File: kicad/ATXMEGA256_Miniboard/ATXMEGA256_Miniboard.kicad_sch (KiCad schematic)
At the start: 26 parts, among them J1 2x5 IDC Socket, J10 1x2 Goldpin Header, J11 2x5 Goldpin Socket, J12 1x2 Goldpin Header, J13 USB micro B 2.0 Socket, J14 2x3 Goldpin Socket, J15 2x3 Goldpin Socket, J2 1x2 Screw Terminal, J3 2x3 Goldpin Header, J4 2x5 Goldpin Socket, J5 2x5 Goldpin Socket, J6 2x5 Goldpin Socket, J7 2x3 Goldpin Socket, J8 2x5 Goldpin Socket, J9 1x2 Goldpin Header, SW1 RESET, U1 ATXMEGA256A3B-AU, Y1 32.768 kHz, Y2 16 MHz

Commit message: rev 1.1
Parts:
- removed J10, J12, J9: 1x2 Goldpin Header, Connector_PinHeader_2.54mm:PinHeader_1x02_P2.54mm_Vertical, symbol Connector:Conn_01x02_Pin
- removed J11, J4, J5, J6, J8: 2x5 Goldpin Socket, Connector_PinSocket_2.54mm:PinSocket_2x05_P2.54mm_Vertical_SMD, symbol Connector_Generic:Conn_02x05_Odd_Even
- removed J13: USB micro B 2.0 Socket, Connector_USB:USB_Micro-B_Amphenol_10118193-0001LF_Horizontal, symbol Connector:USB_B_Micro
- removed J14, J7: 2x3 Goldpin Socket, Connector_PinSocket_2.54mm:PinSocket_2x03_P2.54mm_Vertical_SMD, symbol Connector_Generic:Conn_02x03_Odd_Even
- removed J2: 1x2 Screw Terminal, TerminalBlock:TerminalBlock_bornier-2_P5.08mm, symbol Connector:Screw_Terminal_01x02
- added C1, C2, C3, C4, C5, C7, C8: 100n, Capacitor_SMD:C_0805_2012Metric_Pad1.18x1.45mm_HandSolder, symbol Device:C
- added C6: 10u, Capacitor_SMD:C_1210_3225Metric_Pad1.33x2.70mm_HandSolder, symbol Device:C
- added J1: 1x2 Screw Terminal, TerminalBlock:TerminalBlock_bornier-2_P5.08mm, symbol Connector:Screw_Terminal_01x02
- added J2: 10118192-0001LF, 10118192-0001LF:AMPHENOL_10118192-0001LF, symbol 10118192-0001LF:10118192-0001LF
- added L1: 2u2, Inductor_SMD:L_0805_2012Metric_Pad1.15x1.40mm_HandSolder, symbol Device:L_Ferrite
- JP1, JP2: footprint Jumper:SolderJumper-3_P1.3mm_Bridged12_Pad1.0x1.5mm_NumberLabels -> Jumper:SolderJumper-3_P1.3mm_Bridged12_RoundedPad1.0x1.5mm_NumberLabels
- renumbered C1 to C10, C2 to C11, C3 to C9, J1 to J3, J15 to J4, J3 to J5
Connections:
- net +5V: now also J2.1 (VUSB)
- net D+: now also JP1.1 (A), J2.3 (D+); no longer U1.33 (PD7)
- net D-: now also JP2.1 (A), J2.2 (D-); no longer U1.32 (PD6)
- net GND: now also C1.1, C2.1, C3.1, C4.1, C5.1, C6.1, C7.1, C8.1, J1.1 (Pin_1), J2.5 (GND)
- net VBAT: now also U1.51 (VBAT)
- net ~{RESET}: now also C8.2
- net PD7: now reaches JP1.3 (B)
- net PD6: now reaches JP2.3 (B)
- net at C9.2, R2.1: now also J2.6 (SHIELD)
- net at C10.2, Y2.3: now also U1.58 (PR0); no longer JP1.1 (A)
- net at JP1.2 (C): now also U1.33 (PD7); no longer U1.58 (PR0)
- net at C11.2, Y2.1: now also U1.59 (PR1); no longer JP2.1 (A)
- net at JP2.2 (C): now also U1.32 (PD6); no longer U1.59 (PR1)
- net Power Supply/+3V3_MCU_AVCC: no longer names the net of U1.61 (AVCC)
- net Power Supply/+3V3_MCU_AVCC: now also C6.2, C7.2, L1.2
- net Power Supply/+3V3_MCU_VCC renamed Power Supply/VCC_MCU
- net Power Supply/VCC_MCU: now also C1.2, C2.2, C3.2, C4.2, C5.2, L1.1
- new net Power Supply/VCC_EXT: J1.2 (Pin_2)
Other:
- added sheet GPIO Connectors (gpio_connectors.kicad_sch)
- sheet Power Supply ports: added VCC_EXT, VCC_MCU; removed +3V3, +3V3_MCU_AVCC, +3V3_MCU_VCC, +5V, EXT_VCC
- note added: "Kondensatory odsprzęgające pinów zasilających MCU"
- note added: "Wybór połączenia PD6- PD7: USB/GPIO"
- note added: "Zasilanie części analogowej MCU"
- note removed: "GPIO Bank A"
- note removed: "GPIO Bank B"
- note removed: "GPIO Bank C"
- note removed: "GPIO Bank D"
- note removed: "GPIO Bank E"
- note removed: "GPIO Bank F"
- note removed: "GPIO Bank R"
- note removed: "Punkt pomiaru prądu I_BAT"
- note removed: "Wybór połączenia PB6- PB7: USB/GPIO"
- note removed: "Wybór połączenia PR0 - PR1: XTAL/GPIO"
- moved on the sheet: C10, C11, C9, J3, J4, J5, R1, R2, SW1, U1, Y1, Y2

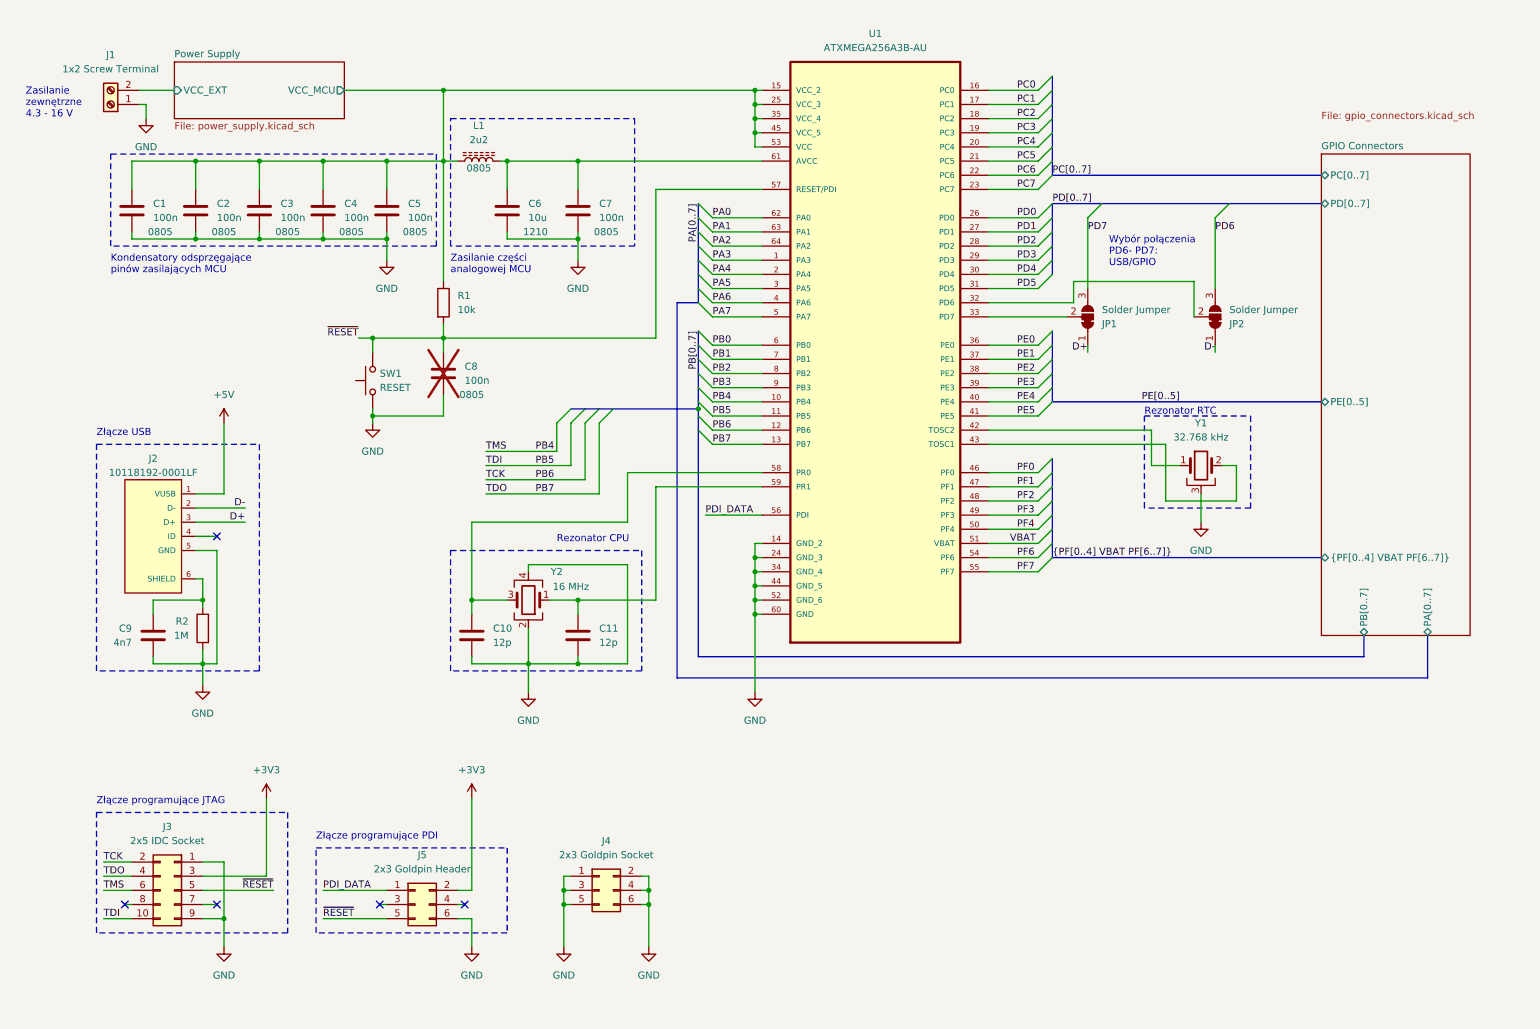
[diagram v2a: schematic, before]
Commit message: Poprawki zasilania, zmiana oscylatora RTC, poprawki polaczen GPIO
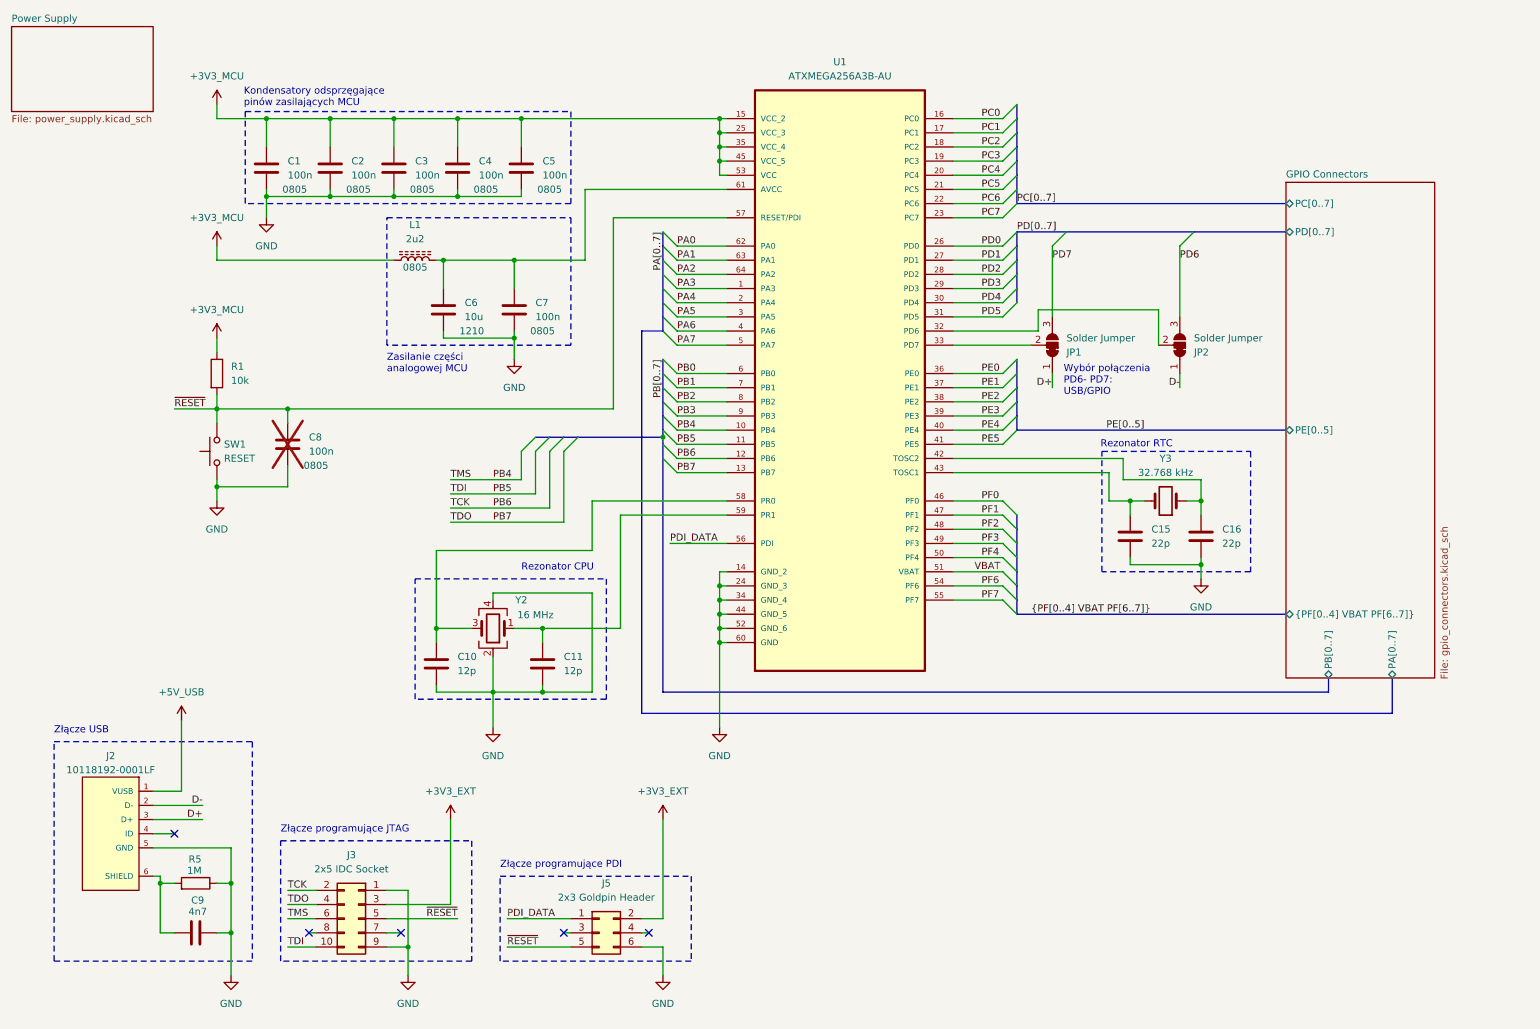
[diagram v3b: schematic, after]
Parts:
- removed J1: 1x2 Screw Terminal, TerminalBlock:TerminalBlock_bornier-2_P5.08mm, symbol Connector:Screw_Terminal_01x02
- removed J4: 2x3 Goldpin Socket, Connector_PinSocket_2.54mm:PinSocket_2x03_P2.54mm_Vertical_SMD, symbol Connector_Generic:Conn_02x03_Odd_Even
- removed R2: 1M, Resistor_SMD:R_0603_1608Metric_Pad0.98x0.95mm_HandSolder, symbol Device:R
- removed Y1: 32.768 kHz, Crystal:Crystal_DS26_D2.0mm_L6.0mm_Horizontal_1EP_style1, symbol Device:Crystal_GND2
- added C15, C16: 22p, Capacitor_SMD:C_0603_1608Metric_Pad1.08x0.95mm_HandSolder, symbol Device:C
- added R5: 1M, Resistor_SMD:R_0603_1608Metric_Pad0.98x0.95mm_HandSolder, symbol Device:R
- added Y3: 32.768 kHz, LFXTAL025159:LFXTAL025159Reel, symbol Device:Crystal
- C10, C11: Part Number C0603C120J5GAC -> C0603C120J5GACTU
- SW1: footprint Button_Switch_SMD:SW_SPST_Omron_B3FS-100xP -> FSM2JSMAA:SW_SMD_2-1437565-8_4_4.50_6.00_6.00_5.00
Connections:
- net GND: now also C15.1, C16.1, R5.1
- net at C9.2, J2.6 (SHIELD): now also R5.2
- net at U1.42 (TOSC2): now also C16.2, Y3.1
- net at U1.43 (TOSC1): now also C15.2, Y3.2
- net +3V3 renamed +3V3_EXT
- net +5V renamed +5V_USB
- net Power Supply/VCC_MCU renamed +3V3_MCU
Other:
- sheet Power Supply ports: added none; removed VCC_EXT, VCC_MCU
- note removed: "Zasilanie zewnętrzne 4.3 - 16 V"
- moved on the sheet: C1, C10, C11, C2, C3, C4, C5, C6, C7, C8, C9, J2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
